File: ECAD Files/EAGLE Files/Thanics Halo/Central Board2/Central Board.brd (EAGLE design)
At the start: 38.6 x 75.4 mm, 69 parts, among them J5 U.FL, J8 MICROSD, U3 LM3880MF-1AA/NOPBMF06A-M, U4 NEO-M8, U5 TPS6209, U7 MIC23050

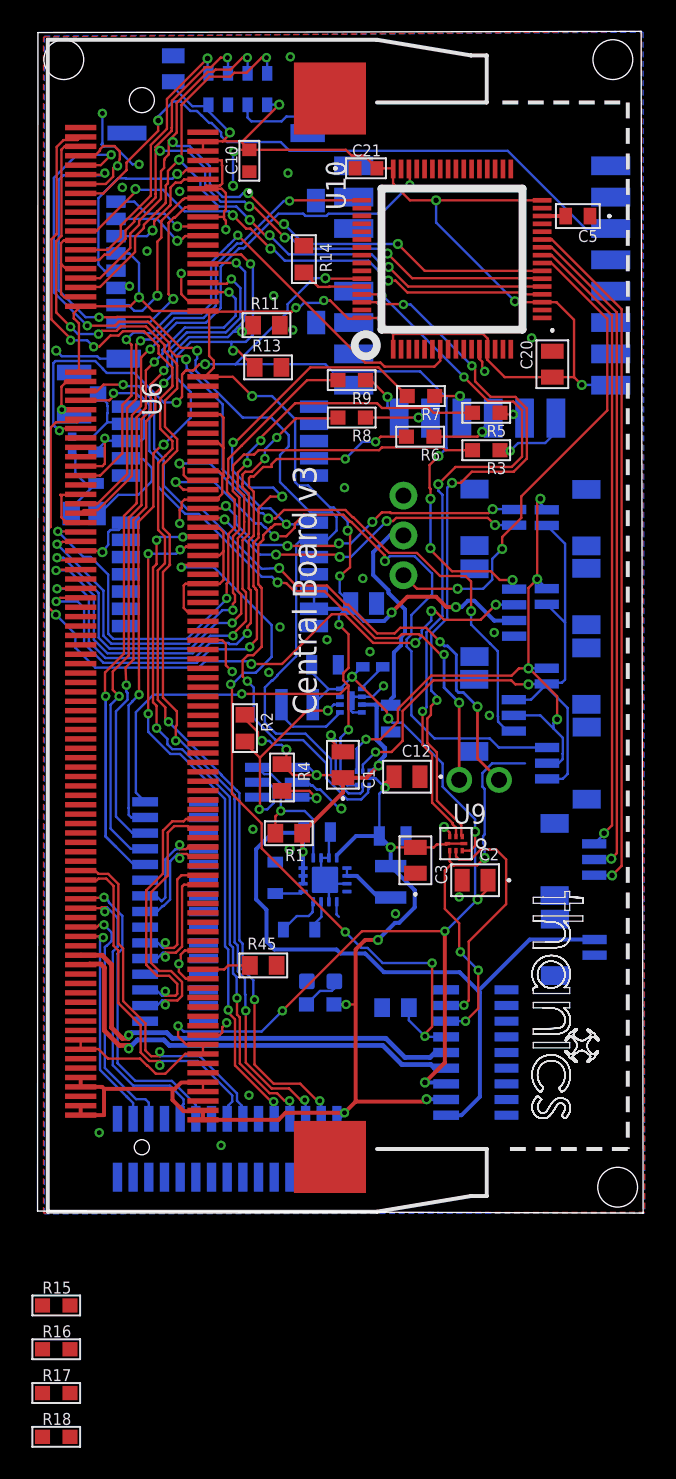
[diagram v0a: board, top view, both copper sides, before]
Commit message: Reorganized ECAD Files
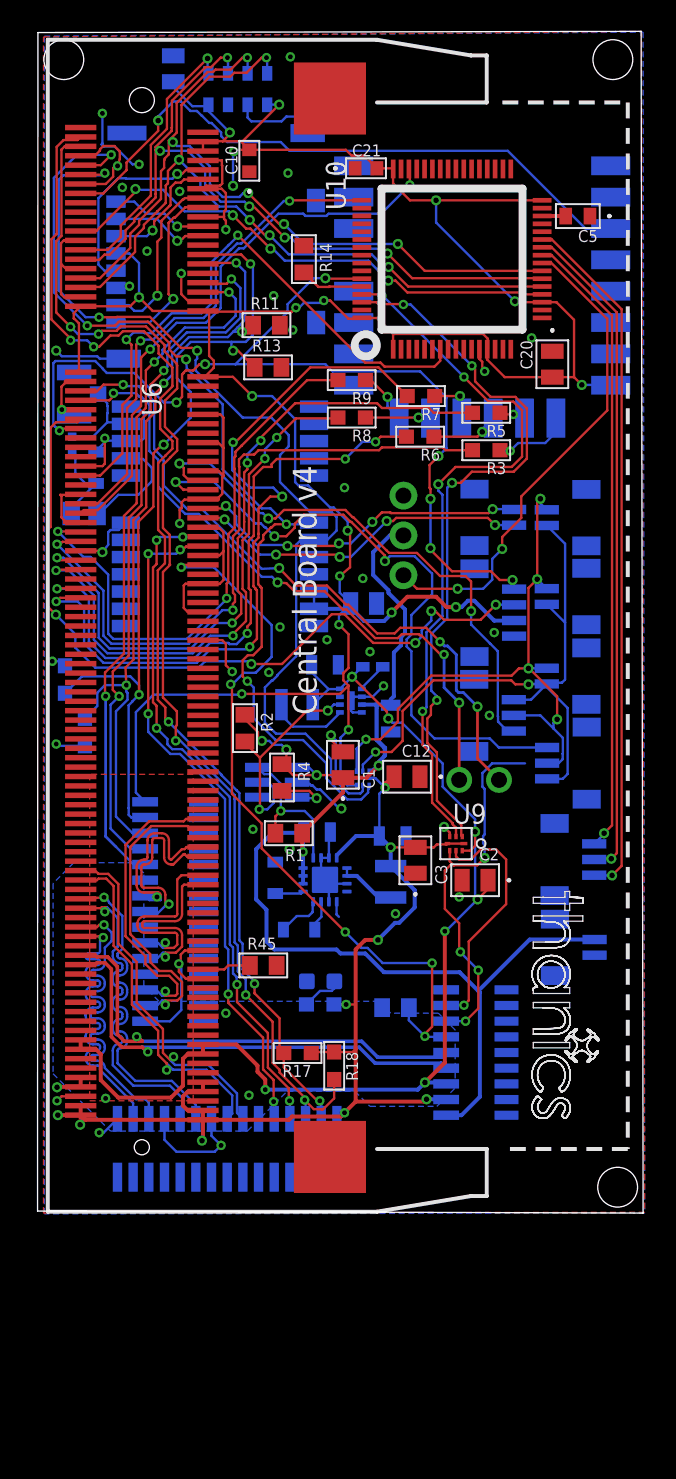
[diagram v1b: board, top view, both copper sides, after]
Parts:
- moved R15 39.9 mm to (17.6, 34.1), flipped to the bottom, turned to 270 degrees
- moved R16 39.4 mm to (18.9, 30.7), flipped to the bottom, turned to 90 degrees
- moved R18 29.6 mm to (34.8, 9.45), turned to 270 degrees
- moved R17 26.6 mm to (32.5, 10.3), turned to 180 degrees
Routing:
- net GND: track 120.3 -> 134.4 mm, vias 42 -> 44
- net C1_D0_N: track 14.2 -> 21.1 mm
- net SDA0: track 48.2 -> 54.2 mm
- net C1_D0_P: track 15.8 -> 21.3 mm
- net C0_C_N: track 7.34 -> 12.7 mm
- net C0_C_P: track 7.27 -> 12.3 mm
- net +3V3: track 260.1 -> 264.7 mm, vias 24 -> 30
- net C0_D1_P: track 8.84 -> 13.2 mm
- net C0_D1_N: track 8.44 -> 12.8 mm
- net SCL0: track 47.3 -> 51.4 mm
- net 1.8V: track 74.4 -> 71.5 mm, vias 8 -> 7
- net SCL1: track 76.0 -> 78.9 mm
- net C1_D1_N: track 19.6 -> 21.6 mm
- net C1_D1_P: track 19.7 -> 21.7 mm
- net C0_D0_P: track 17.8 -> 19.8 mm
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- added copper zone on layer 15, net +3V3
- added copper zone on layer 2, net GND
- added copper zone on layer 1, net N$17
- added copper zone on layer 16, net N$18
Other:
- board text added: "Central Board v4"
- board text removed: "Central Board v3"
